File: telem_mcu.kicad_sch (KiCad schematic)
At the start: 21 parts, among them J3 Conn_01x06, SW2 SW_Push, SW3 SW_SPDT, U3 STM32F373CCTx, X1 32.768kHz

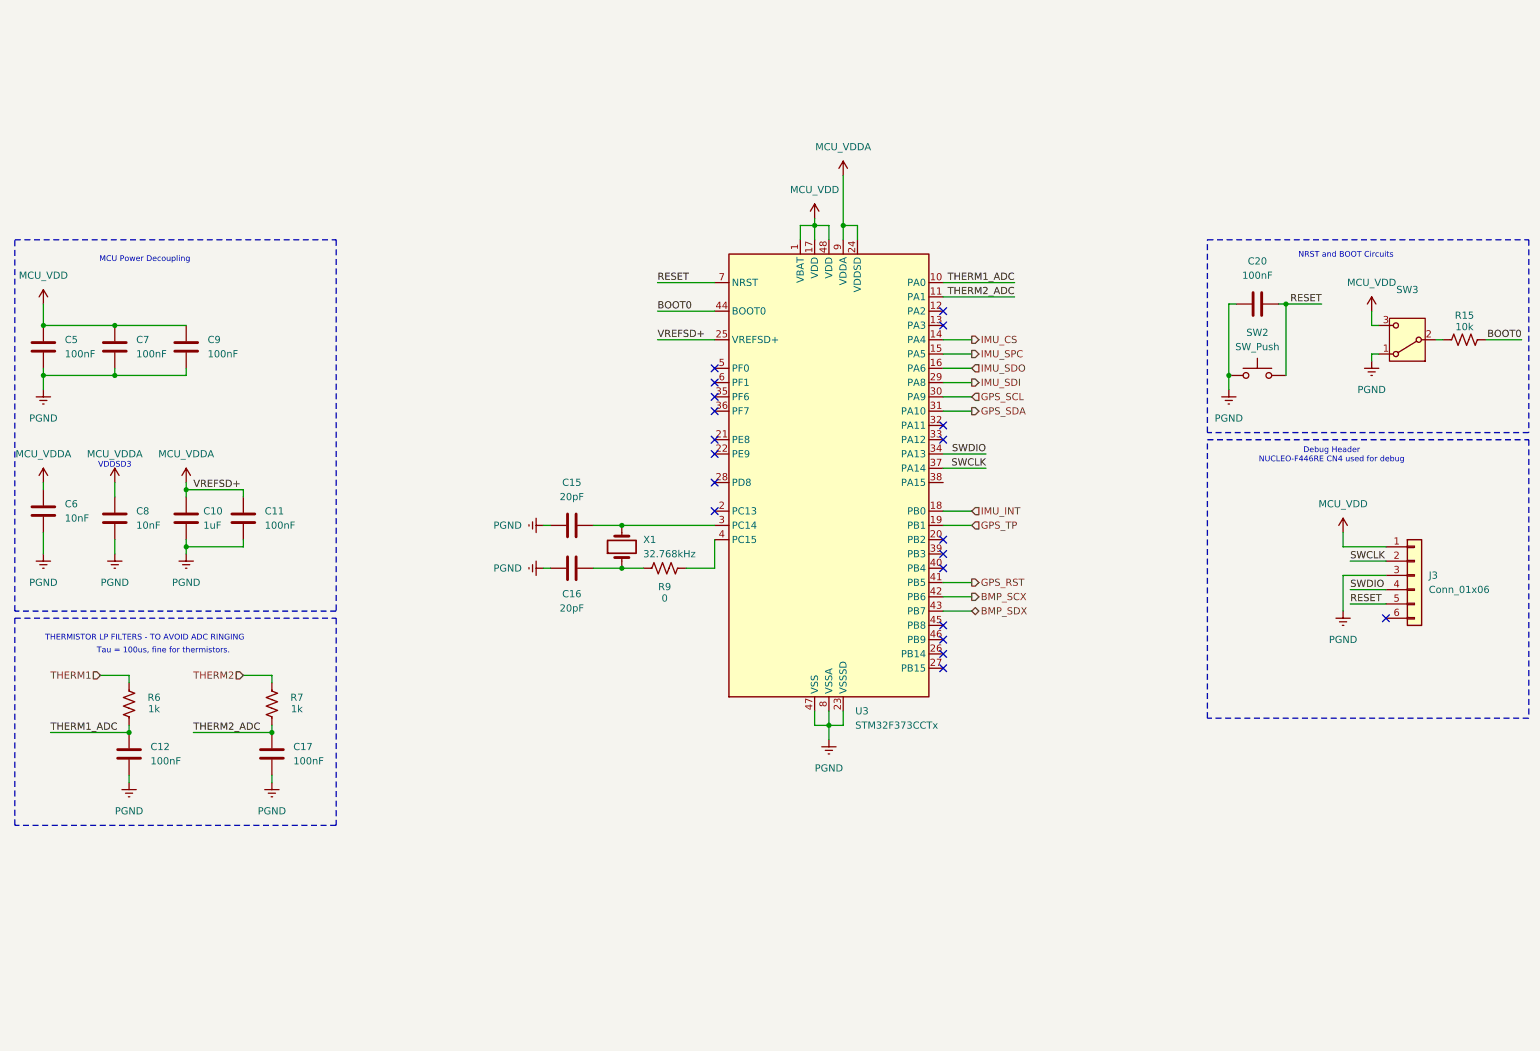
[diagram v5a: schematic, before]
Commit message: Updated schematics to add SD, will finish SD next and redo layout
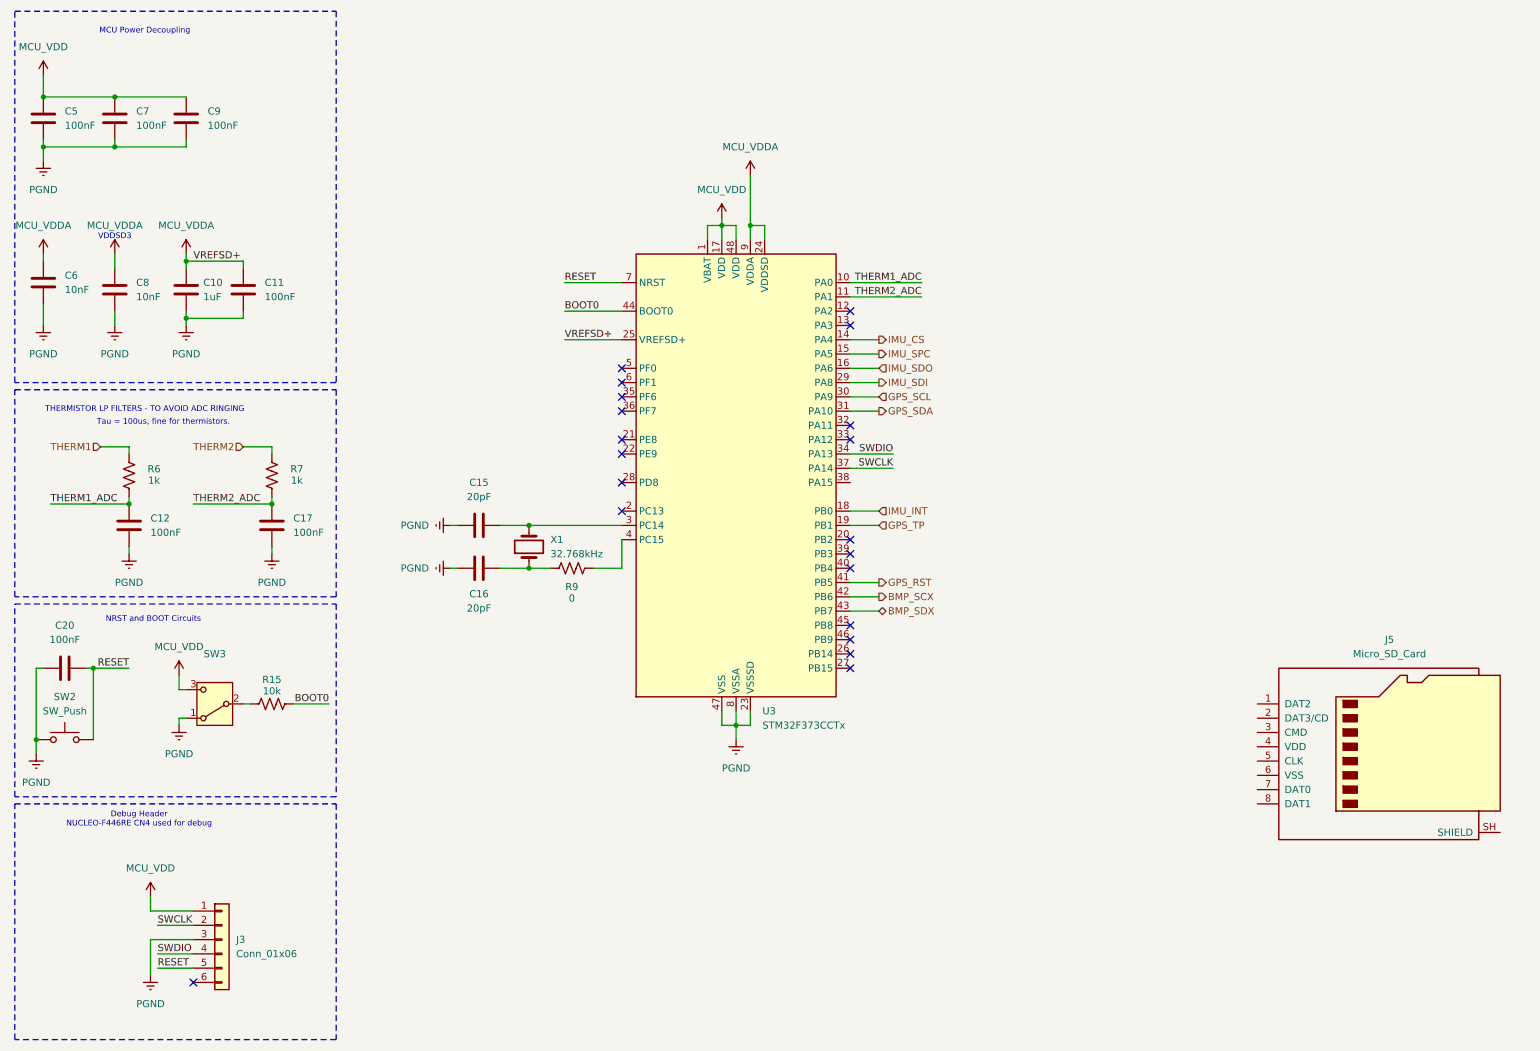
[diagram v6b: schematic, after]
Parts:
- added J5: Micro_SD_Card, Connector_Card:microSD_HC_Molex_47219-2001, symbol Connector:Micro_SD_Card
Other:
- moved on the sheet: C10, C11, C12, C15, C16, C17, C20, C5, C6, C7, C8, C9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

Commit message: Rev1 final commit
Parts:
- removed SW3: SW_SPDT, Telem_fp:SWITCH_1SCQN, symbol Switch:SW_SPDT
- added C18: 100nF, Capacitor_SMD:C_0603_1608Metric, symbol Device:C
- added R10, R11, R12, R13, R14, R8: 2k2, Resistor_SMD:R_0603_1608Metric, symbol Device:R_US
- C12, C17: footprint Capacitor_SMD:C_0805_2012Metric -> Capacitor_SMD:C_0603_1608Metric
- J5: footprint Connector_Card:microSD_HC_Molex_47219-2001 -> Telem_fp:AMPHENOL_10067099-200LF
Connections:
- net MCU_VDD is gone; now on net +3V3: C5.1, C7.1, C9.1, J3.1 (Pin_1), U3.1 (VBAT), U3.17 (VDD), U3.48 (VDD)
- net MCU_VDDA is gone; now on net +3V3: C10.1, C11.1, C6.1, C8.1, U3.24 (VDDSD), U3.25 (VREFSD+), U3.9 (VDDA)
- net BMP_SCX: now also R11.1
- net BMP_SDX: now also R12.1
- net GPS_SCL: now also R8.1
- net GPS_SDA: now also R10.1
- net IMU_CS: now also R13.1
- net PGND: now also J5.6 (VSS), J5.SH (SHIELD), R15.1, C18.2
- net SD_CS: now reaches J5.2 (DAT3/CD)
- net SD_CS: now also U3.46 (PB9), R14.1
- net SD_MOSI: now reaches J5.3 (CMD)
- net SD_MOSI: now also U3.27 (PB15)
- net +3V3: now reaches J5.4 (VDD)
- net +3V3: now also C18.1, R10.2, R11.2, R12.2, R13.2, R14.2, R8.2
- net SD_CLK: now reaches J5.5 (CLK)
- net SD_CLK: now also U3.45 (PB8)
- net SD_MISO: now reaches J5.7 (DAT0)
- net SD_MISO: now also U3.26 (PB14)
- no-connect marks 20 -> 18
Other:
- note added: "NRST Circuit"
- note added: "Pullup Resistors"
- note removed: "NRST and BOOT Circuits"
- moved on the sheet: C20, J5, R15, SW2
